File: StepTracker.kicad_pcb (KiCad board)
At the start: 2 copper layers, 28.5 x 29 mm, 31 parts, among them J1 Conn_01x02, J2 USB-TYPE-C-008, J3 Conn_ARM_SWD_TagConnect_TC203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, U1 MDBT50Q-512K, U2 TLV70033_SOT23-5, U3 LSM6DSOXTR, U6 BQ24079RGT, Y1 Crystal

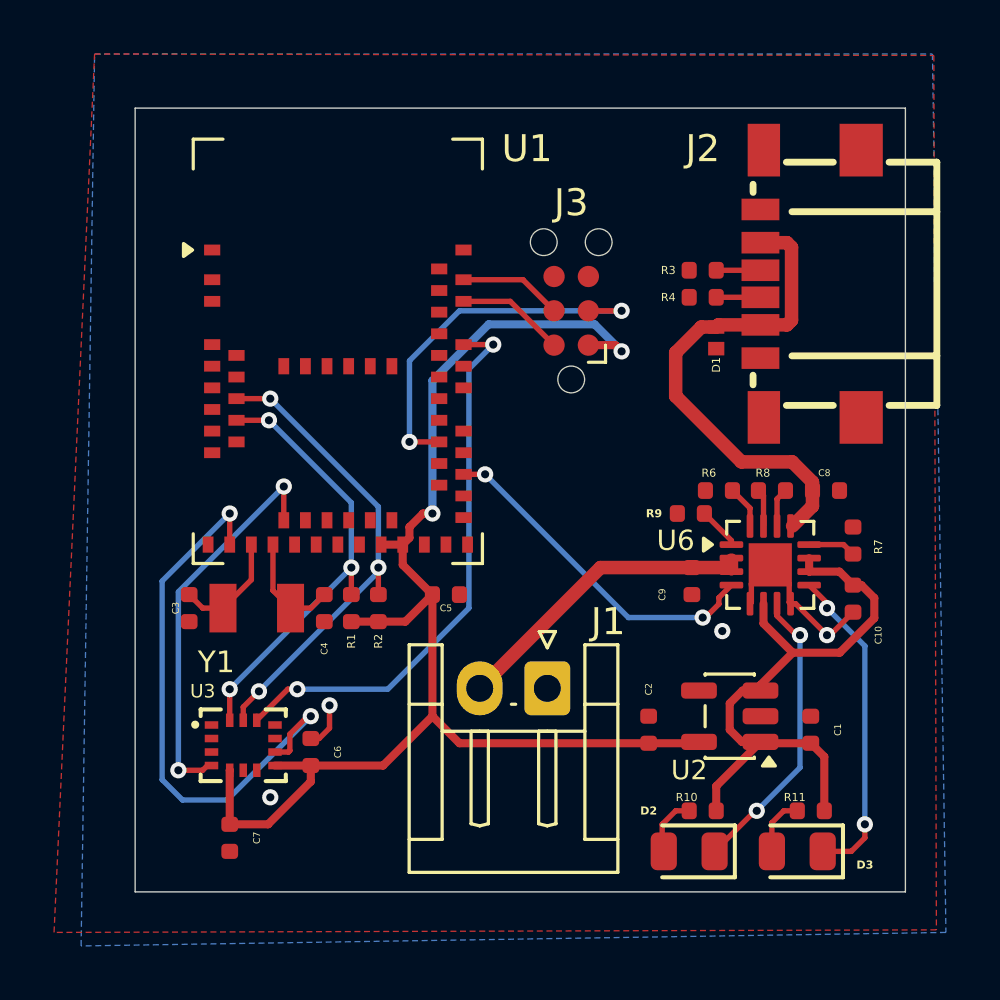
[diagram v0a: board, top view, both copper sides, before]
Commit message: update to include footprints from project specific lib
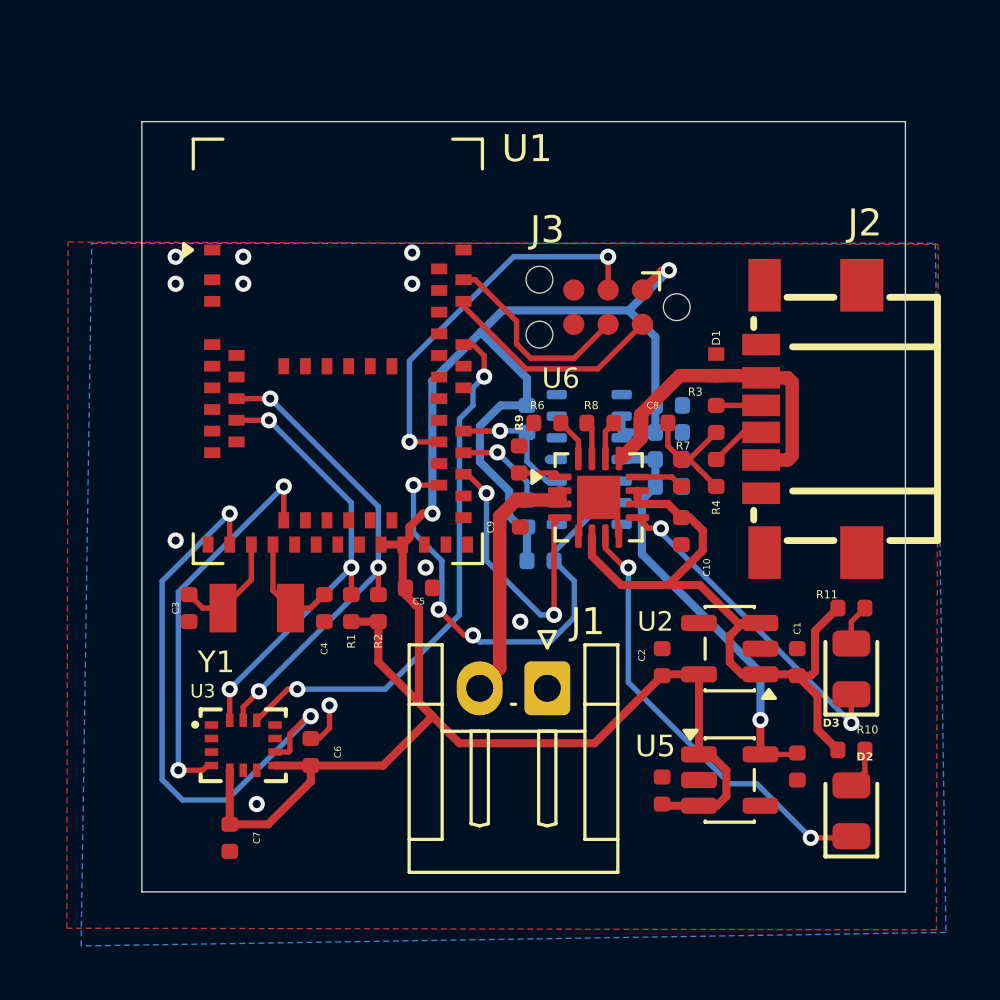
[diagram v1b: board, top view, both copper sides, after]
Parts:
- added C11: 1 uF, PCM_JLCPCB:C_0402, F.Cu at (187.0, 77.8)
- added C12: 1 uF, PCM_JLCPCB:C_0402, F.Cu at (192.0, 76.9)
- added C13: 4.7 uF, PCM_JLCPCB:C_0402, B.Cu at (187.2, 66.5)
- added C14: 0.1 uF, PCM_JLCPCB:C_0402, B.Cu at (187.2, 65.5)
- added C15: 10 uF, PCM_JLCPCB:C_0402, B.Cu at (187.2, 63.5)
- added C16: 0.1 uF, PCM_JLCPCB:C_0402, B.Cu at (187.2, 64.5)
- added R12: 1k, PCM_JLCPCB:R_0402, B.Cu at (182.0, 64.0)
- added R13: 1k, PCM_JLCPCB:R_0402, B.Cu at (182.5, 69.2)
- added R5: 1k, PCM_JLCPCB:R_0402, B.Cu at (182.0, 67.5)
- added U4: MAX30102, OptoDevice:Maxim_OLGA-14_3.3x5.6mm_P0.8mm, B.Cu at (184.3, 65.5)
- added U5: TLV70018_SOT23-5, Package_TO_SOT_SMD:SOT-23-5, F.Cu at (189.5, 77.4)
- C1, C2: value 0.1 uF -> 1 uF
- moved R11 7.65 mm to (194.0, 71.0), turned to 180 degrees
- moved D3 7.04 mm to (194.0, 73.2), turned to 90 degrees
- moved C10 6.82 mm to (187.7, 68.2)
- moved C8 6.82 mm to (186.7, 64.2)
- moved C9 6.82 mm to (181.8, 67.5)
- moved R6 6.82 mm to (182.8, 64.2)
- moved R7 6.82 mm to (187.7, 66.0)
- moved R8 6.82 mm to (184.7, 64.2)
- moved U6 6.82 mm to (184.7, 66.9)
- moved R9 6.66 mm to (181.7, 65.5), turned to 90 degrees
- moved R4 6.52 mm to (189.0, 66.0), turned to -90 degrees
- moved D2 6.18 mm to (194.0, 78.5), turned to 90 degrees
- moved R10 5.94 mm to (194.0, 76.2), turned to 180 degrees
- moved R3 5.52 mm to (189.0, 64.0), turned to -90 degrees
- moved J2 5.00 mm to (192.5, 64.0)
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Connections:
- net /SOC/SCL renamed /SOC/I2C1_SCL
- net /SOC/SDA renamed /SOC/I2C1_SDA
- U1 pad 36: unconnected-(U1-P0.14-Pad36) -> /SOC/HR_INT
- U1 pad 39: unconnected-(U1-P0.15-Pad39) -> /SOC/I2C2_SCL
- U1 pad 41: unconnected-(U1-P0.17-Pad41) -> /SOC/I2C2_SDA
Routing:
- net 3.3V: track 50.5 -> 81.9 mm
- net /SOC/HR_INT: track 0.00 -> 17.6 mm, vias 0 -> 3
- net 1.8V: track 0.00 -> 15.5 mm, vias 0 -> 1
- net /Power/USB_5V: track 18.6 -> 12.1 mm
- net Net-(U6-~{PGOOD}): track 10.9 -> 16.5 mm
- net /SOC/I2C2_SDA: track 0.00 -> 4.86 mm, vias 0 -> 1
- net /SOC/I2C2_SCL: track 0.00 -> 4.62 mm, vias 0 -> 1
- net /SOC/SWDIO: track 4.02 -> 8.45 mm
- net /SOC/SWCLK: track 3.83 -> 7.56 mm
- net /Power/VChrg: track 23.2 -> 25.7 mm
- net ChargeEnable: track 12.7 -> 10.7 mm
- net /Power/VBat: track 11.6 -> 9.56 mm
- net GND: track 9.73 -> 11.4 mm, vias 4 -> 11
- net /SOC/CS_IMU: track 20.9 -> 20.2 mm
- net Net-(D3-Pad2): track 2.18 -> 1.52 mm
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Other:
- board size 28.5 x 29 mm -> 28.2 x 28.5 mm
